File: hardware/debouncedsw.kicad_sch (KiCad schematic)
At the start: 4 parts, among them SW2 SW_Push_6x6

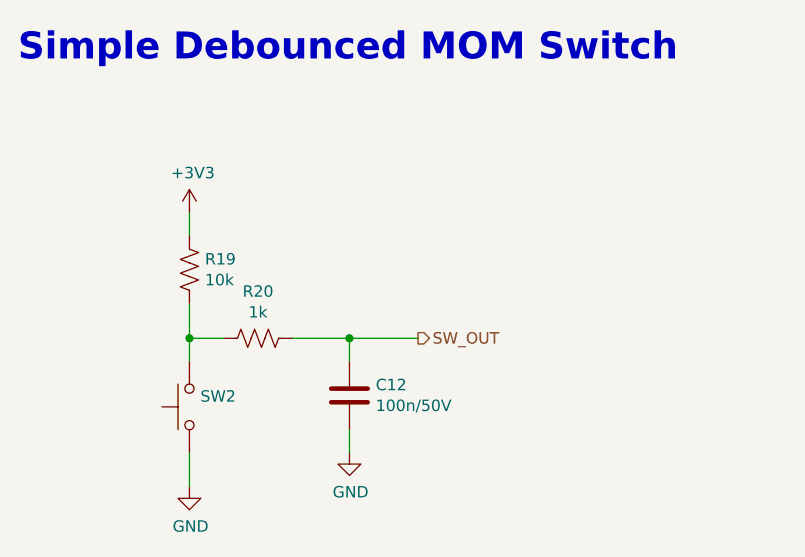
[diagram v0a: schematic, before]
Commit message: v1.2: fixes for vdd and a6/a7 pins
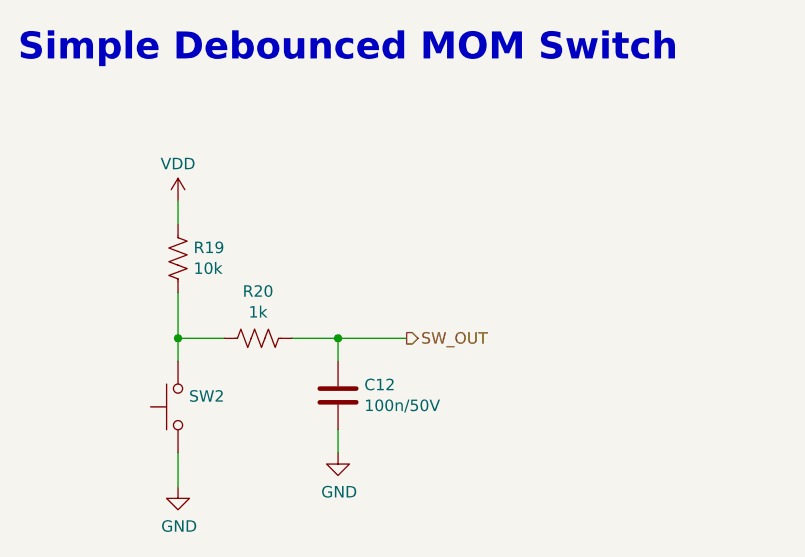
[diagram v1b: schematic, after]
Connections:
- net +3V3 renamed VDD
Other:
- moved on the sheet: C12, R19, SW2

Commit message: Added BOM
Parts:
- SW2: Display Value (none) -> SW_Push; Display value SW_Push -> (none)
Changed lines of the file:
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@@
       (effects (font (size 1.27 1.27)) hide)
     )
-    (property "Display value" "SW_Push" (at 64.7192 62.103 90)
+    (property "Display Value" "SW_Push" (at 64.7192 62.103 90)
       (effects (font (size 1.27 1.27)) (justify right) hide)
     )
